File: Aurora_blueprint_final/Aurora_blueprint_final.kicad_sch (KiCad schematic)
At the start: 29 parts, among them J1 Raspberry_Pi_4, K1 FINDER-40.11, K2 FINDER-40.11, K3 FINDER-40.11, K4 FINDER-40.11, M1 Motor_DC, M2 Motor_DC, M3 Motor_DC, M4 Motor_DC, U1 L7805, U2 L7812, U3 L7805, U4 L7805, U5 L7805, U6 L7812, U7 L7812, U8 L7812

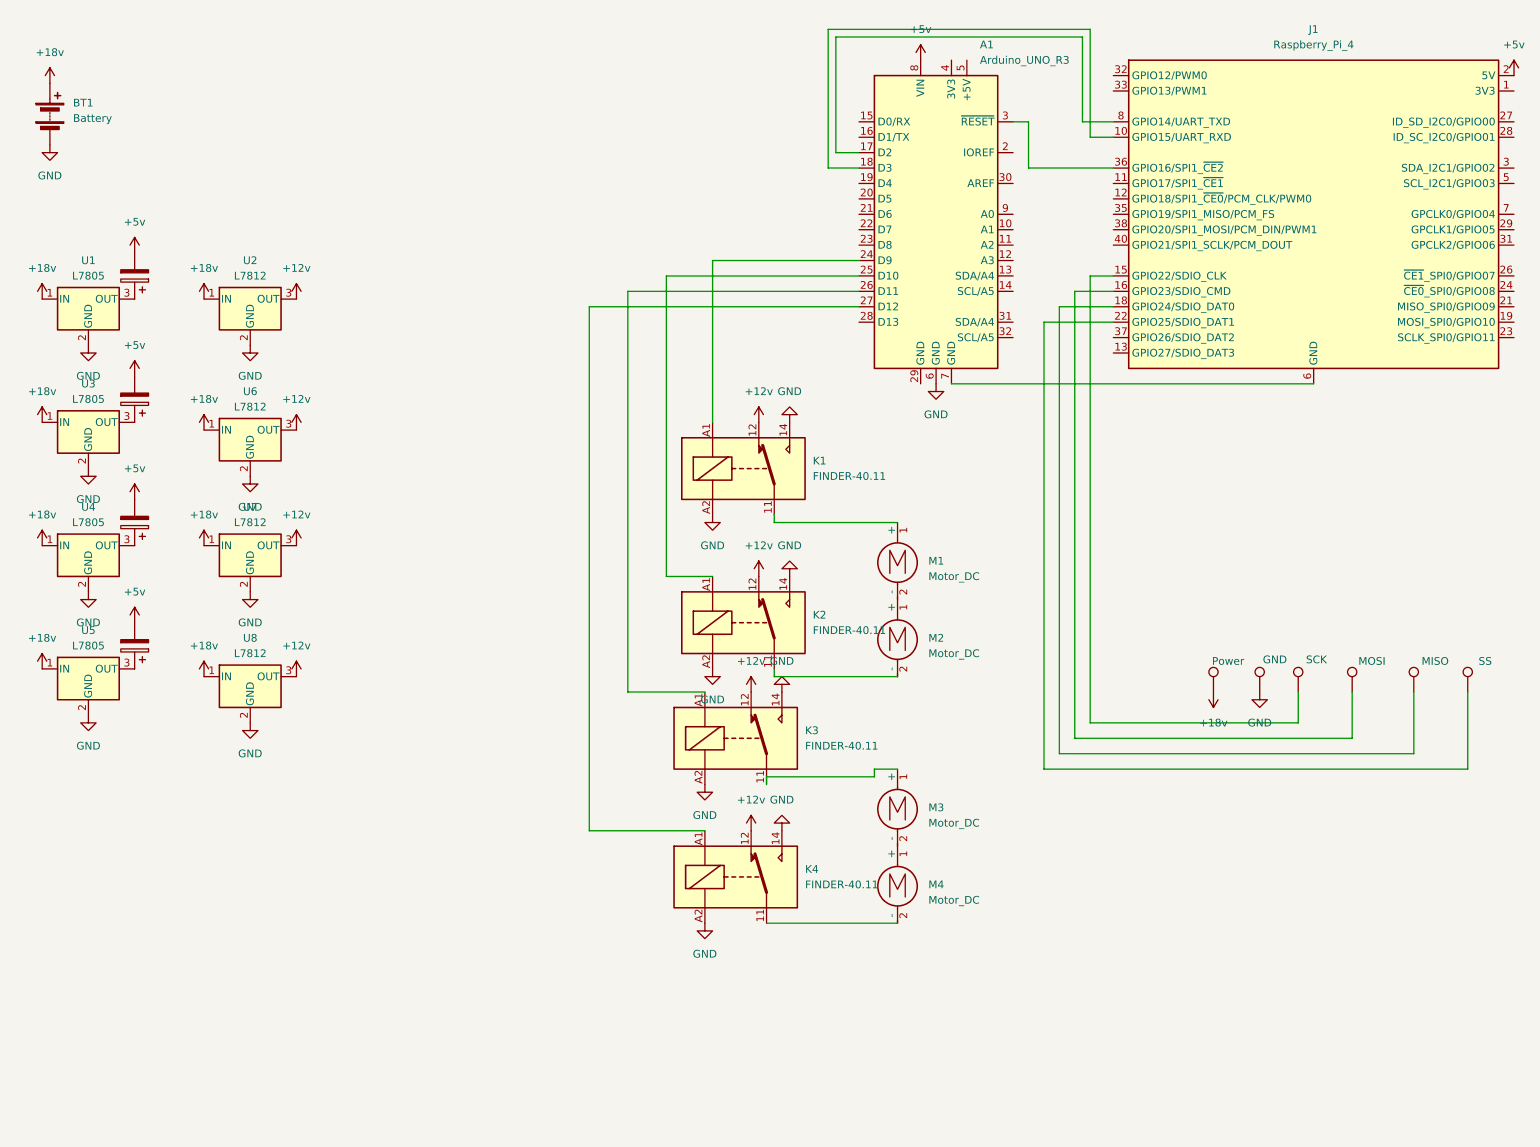
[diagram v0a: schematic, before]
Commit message: Added speedcontrol with arduino provided DPDT relays
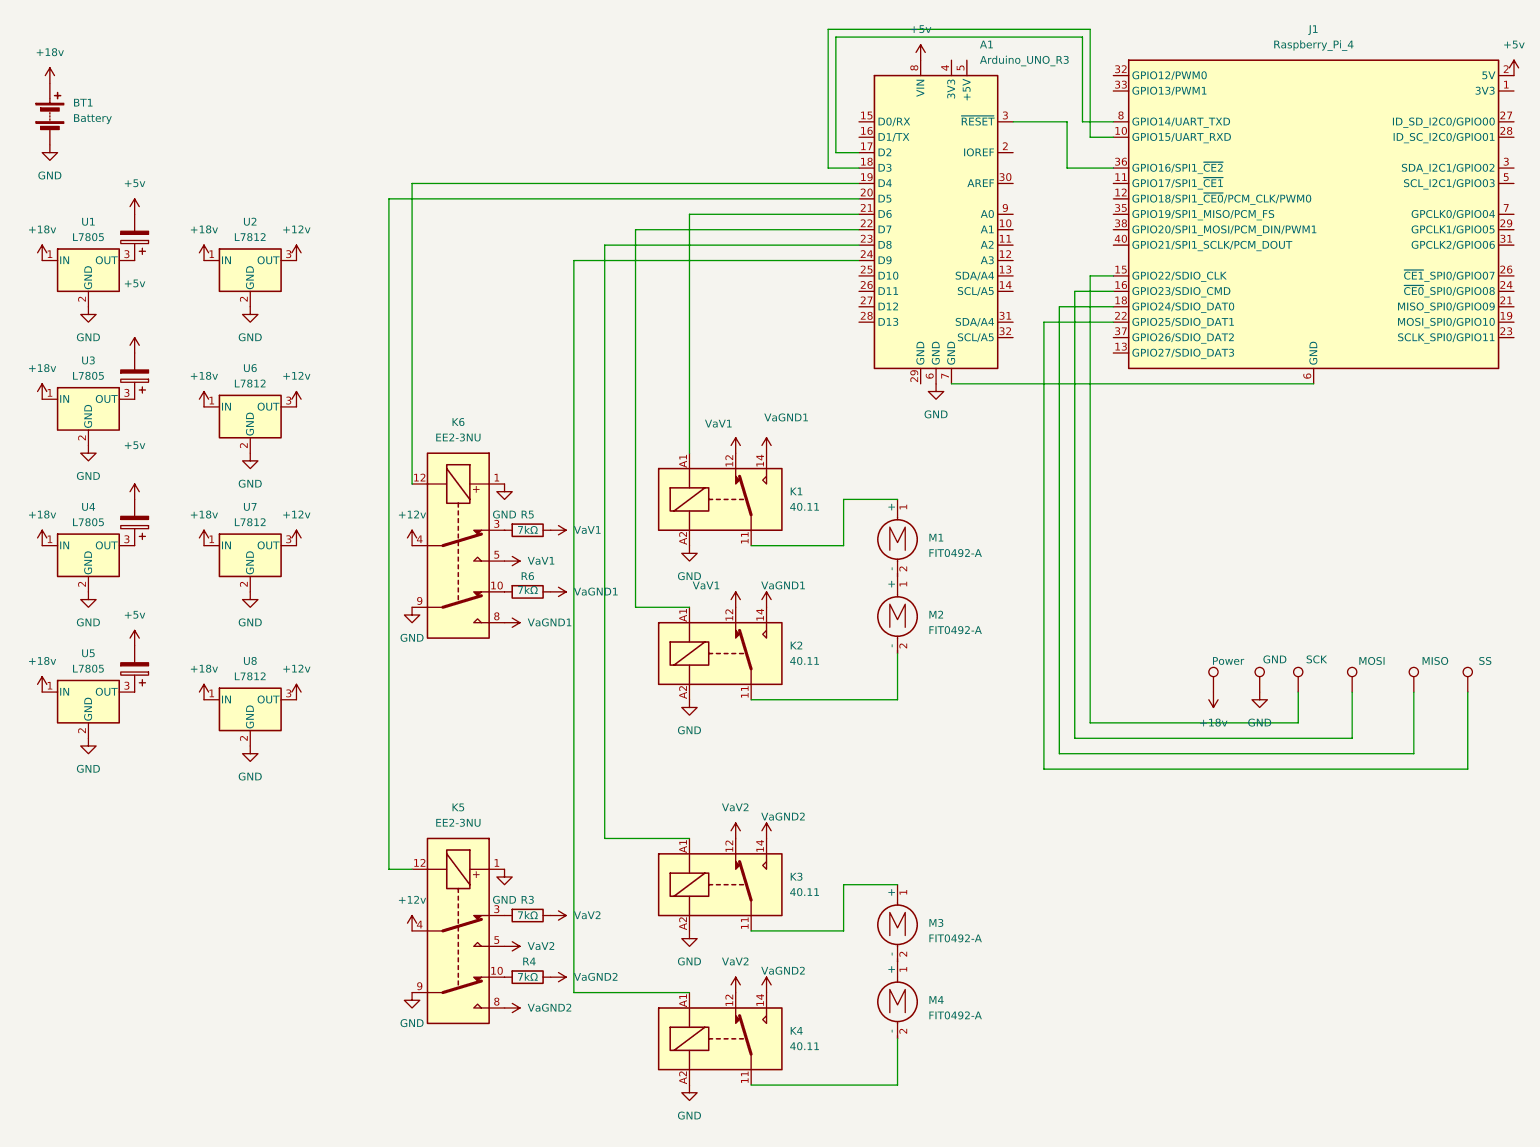
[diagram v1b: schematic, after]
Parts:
- added K5, K6: EE2-3NU, Relay_SMD:Relay_DPDT_Kemet_EE2_NU, symbol Relay:EE2-3NU
- added R3, R4, R5, R6: 7kΩ, symbol Device:R
- K1, K2, K3, K4: value FINDER-40.11 -> 40.11
- M1, M2, M3, M4: value Motor_DC -> FIT0492-A
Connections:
- net +12v: now also K5.4, K6.4; no longer K1.12, K2.12, K3.12, K4.12
- net GND: now also K5.1, K5.9, K6.1, K6.9; no longer K1.14, K2.14, K3.14, K4.14
- net at A1.19 (D4): now also K6.12
- net at A1.20 (D5): now also K5.12
- net at A1.21 (D6): now also K1.A1
- net at A1.22 (D7): now also K2.A1
- net at A1.23 (D8): now also K3.A1
- net at A1.24 (D9): now also K4.A1; no longer K1.A1
- net at A1.25 (D10): no longer K2.A1
- net at A1.26 (D11): no longer K3.A1
- net at A1.27 (D12): no longer K4.A1
- new net: K6.10, R6.2
- new net: K6.3, R5.2
- new net: K5.3, R3.2
- new net: K5.10, R4.2
- new net VaGND1: K1.14, K2.14, K6.8, R6.1
- new net VaGND2: K3.14, K4.14, K5.8, R4.1
- new net VaV1: K1.12, K2.12, K6.5, R5.1
- new net VaV2: K3.12, K4.12, K5.5, R3.1
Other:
- moved on the sheet: K3, K4, M3, M4, U1, U2, U3, U5, U6, U8

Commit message: Stripped arduino of unneeded pins for easier development
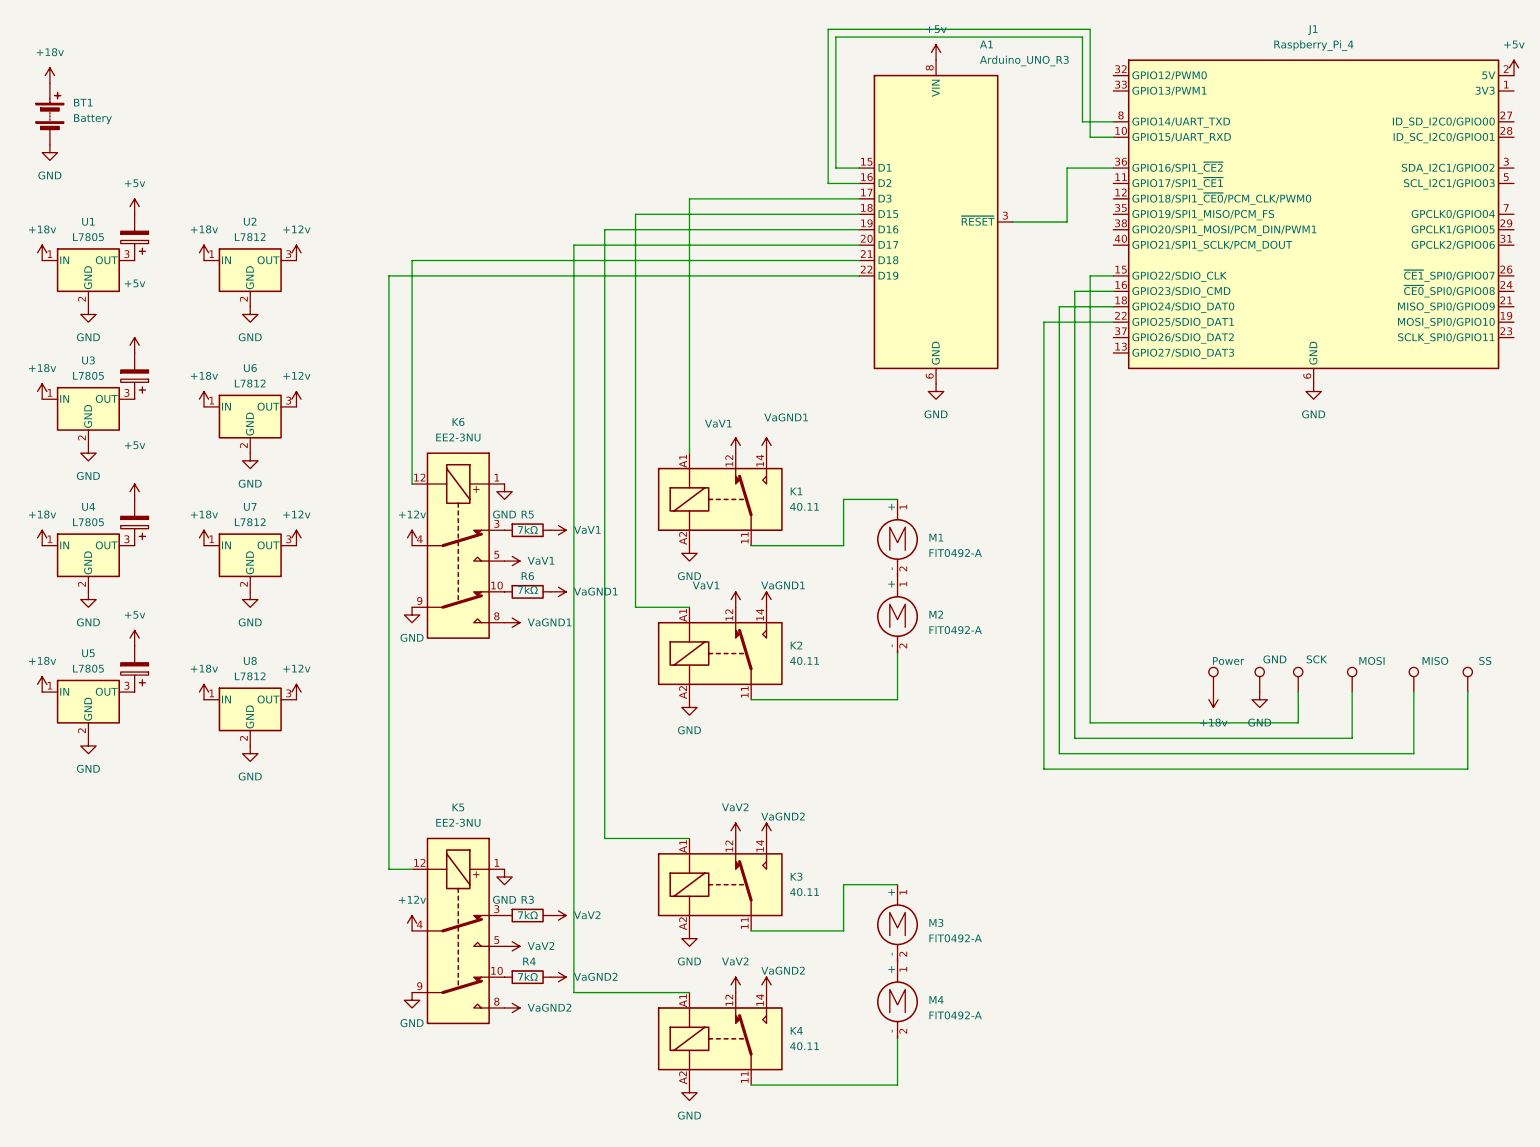
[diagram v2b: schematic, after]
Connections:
- net GND: now also J1.14 (GND), J1.20 (GND), J1.25 (GND), J1.30 (GND), J1.34 (GND), J1.39 (GND), J1.6 (GND), J1.9 (GND)
- net at A1.15 (D1): now also J1.8 (GPIO14/UART_TXD)
- net at A1.16 (D2): now also J1.10 (GPIO15/UART_RXD)
- net at A1.17 (D3): now also K1.A1; no longer J1.8 (GPIO14/UART_TXD)
- net at A1.18 (D15): now also K2.A1; no longer J1.10 (GPIO15/UART_RXD)
- net at A1.19 (D16): now also K3.A1; no longer K6.12
- net at A1.20 (D17): now also K4.A1; no longer K5.12
- net at A1.21 (D18): now also K6.12; no longer K1.A1
- net at A1.22 (D19): now also K5.12; no longer K2.A1

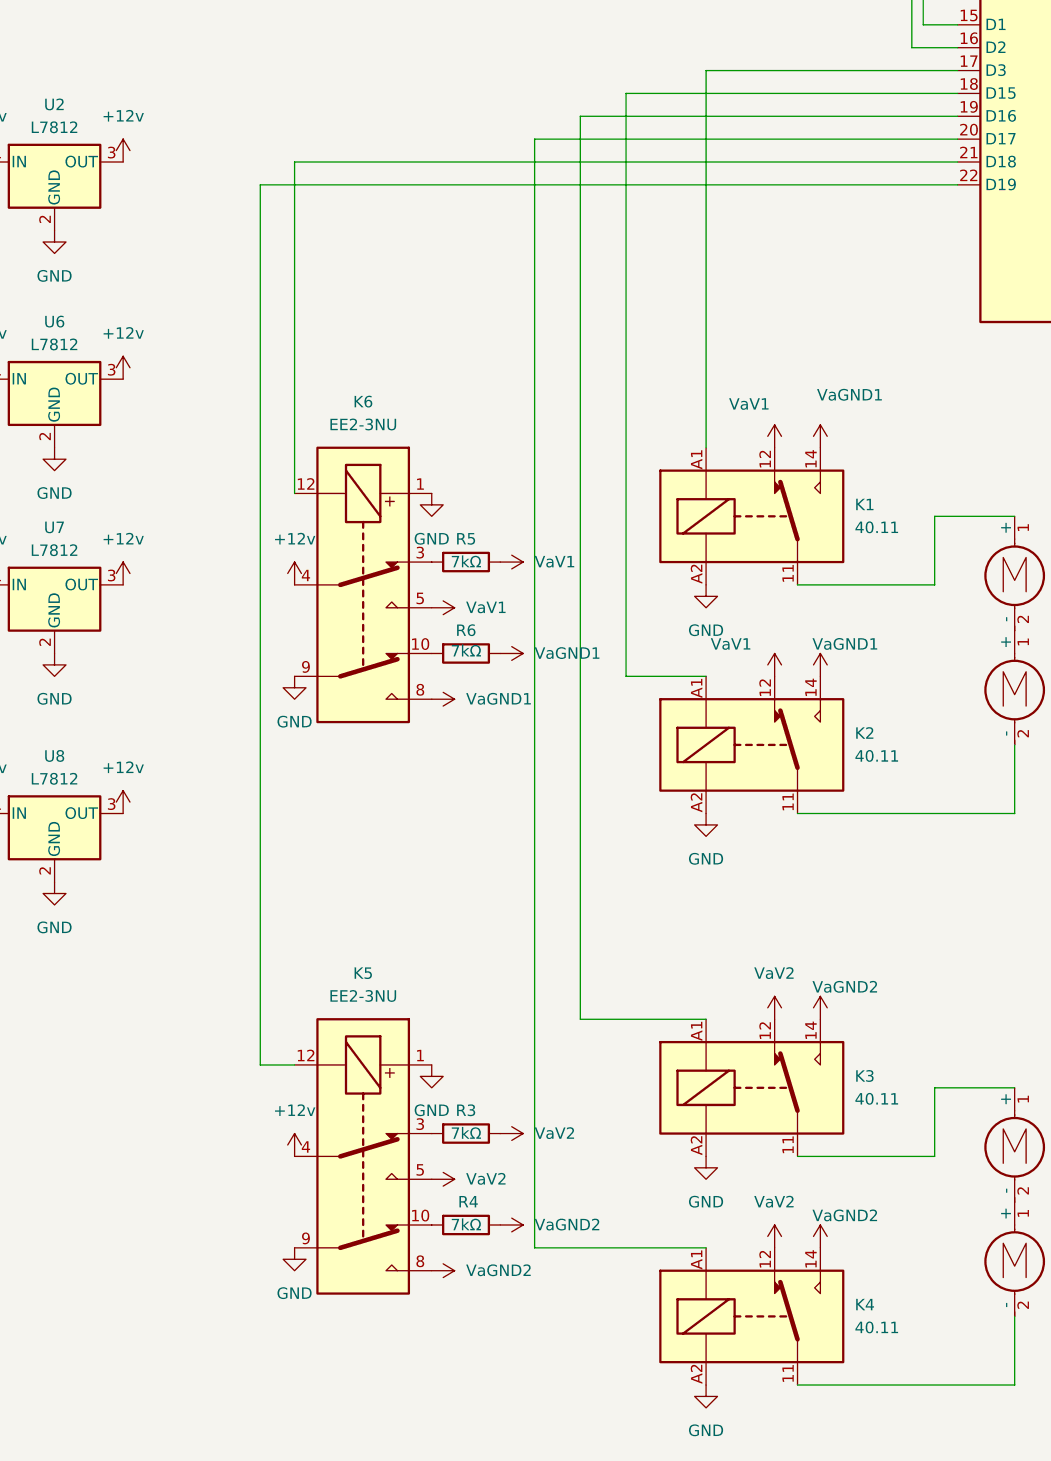
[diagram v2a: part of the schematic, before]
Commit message: Updated cad drawing for better visual clarity
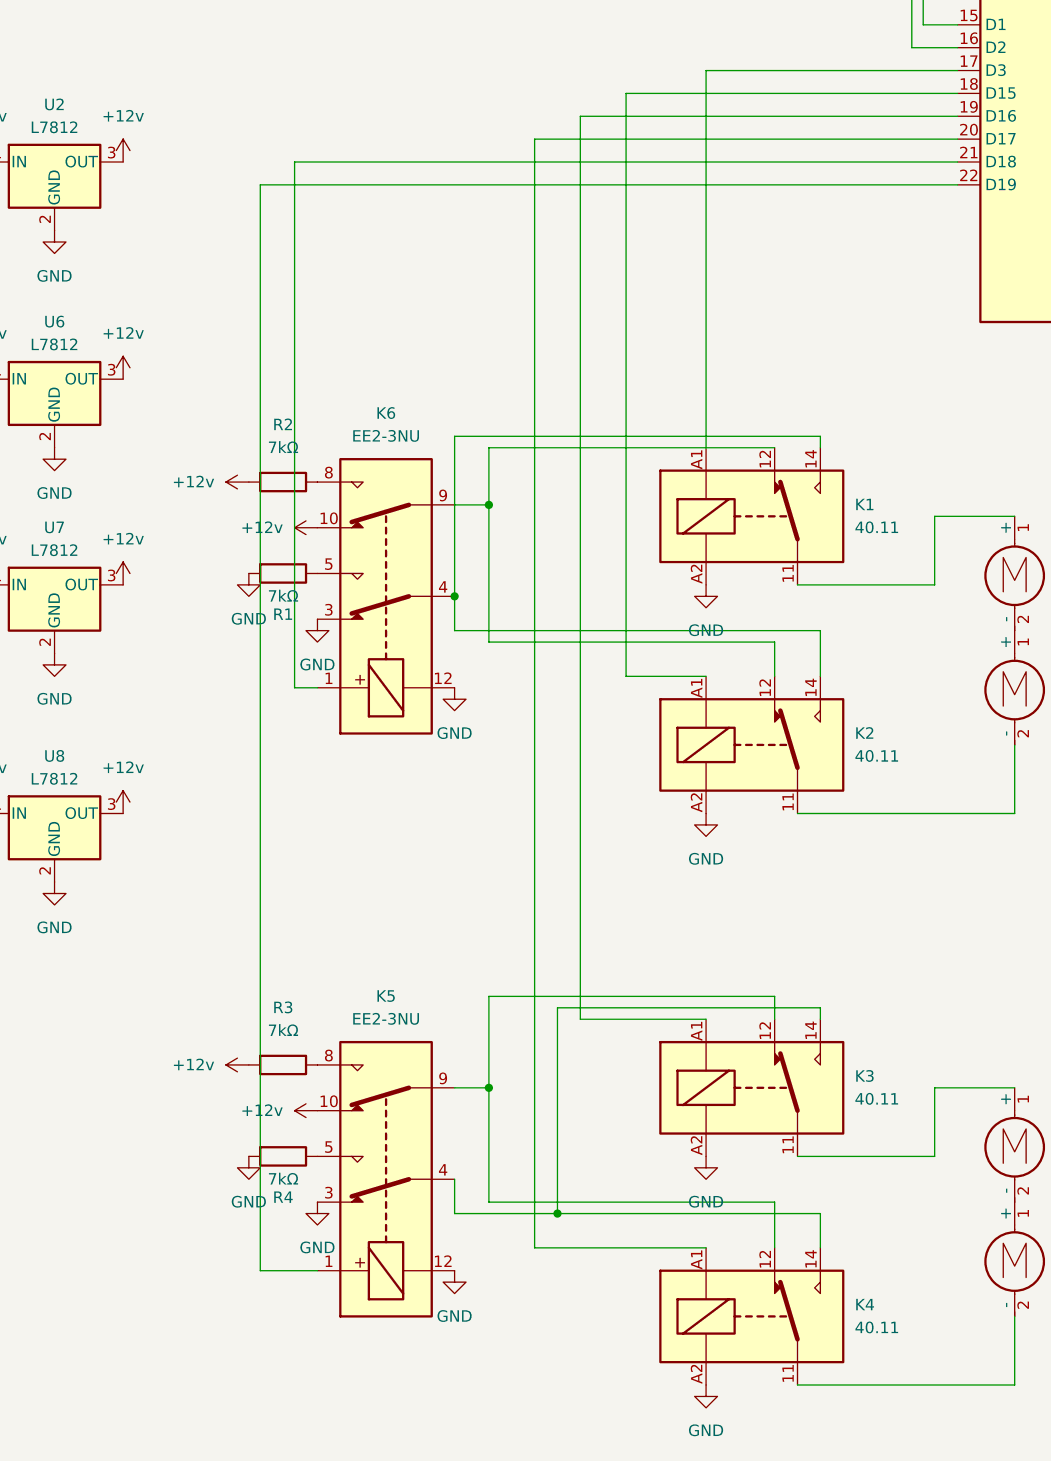
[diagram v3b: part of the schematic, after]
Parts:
- removed R5, R6: 7kΩ, symbol Device:R
- added R1, R2: 7kΩ, symbol Device:R
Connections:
- net +12v: now also K5.10, K6.10, R3.2, R2.2; no longer K5.4, K6.4
- net GND: now also K5.12, K5.3, K6.12, K6.3, R4.2, R1.2; no longer K5.1, K5.9, K6.1, K6.9
- net at A1.21 (D18): now also K6.1; no longer K6.12
- net at A1.22 (D19): now also K5.1; no longer K5.12
- net VaGND1: no longer names the net of K1.14, K2.14
- net VaGND1: now also K6.4; no longer K6.8
- net VaGND2: no longer names the net of K3.14, K4.14
- net VaGND2: now also K5.4; no longer K5.8, R4.1
- net VaV1: no longer names the net of K1.12, K2.12
- net VaV1: now also K6.9; no longer K6.5
- net VaV2: no longer names the net of K3.12, K4.12
- net VaV2: now also K5.9; no longer K5.5, R3.1
- new net: K6.5, R1.1
- new net: K6.8, R2.1
- new net: K5.5, R4.1
- new net: K5.8, R3.1
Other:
- moved on the sheet: K6

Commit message: Revised blueprint
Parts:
- removed A1: Arduino_UNO_R3, Module:Arduino_UNO_R3, symbol MCU_Module:Arduino_UNO_R3
- removed C1, C2, C3, C4: C_Polarized, symbol Device:C_Polarized
- removed GND, MISO, MOSI, SCK, SS: TestPoint, symbol Connector:TestPoint
- removed J1: Raspberry_Pi_4, symbol Connector:Raspberry_Pi_4
- removed K1, K2, K3, K4: 40.11, Relay_THT:Relay_SPDT_Finder_40.11, symbol Relay:FINDER-40.11
- removed K5, K6: EE2-3NU, Relay_SMD:Relay_DPDT_Kemet_EE2_NU, symbol Relay:EE2-3NU
- removed M1, M2, M3, M4: FIT0492-A, symbol Motor:Motor_DC
- removed Power: ~, symbol Connector:TestPoint
- removed R1, R2, R3, R4: 7kΩ, symbol Device:R
- removed U1, U3, U4, U5: L7805, symbol Regulator_Linear:L7805
- removed U2, U6, U7, U8: L7812, symbol Regulator_Linear:L7812
- added A2: Arduino_UNO_R3, Module:Arduino_UNO_R3, symbol MCU_Module:Arduino_UNO_R3
- added BT2: Battery, symbol Device:Battery
- added J2: Raspberry_Pi_4, symbol Connector:Raspberry_Pi_4
- added K10, K11, K7, K8: 40.11, Relay_THT:Relay_SPDT_Finder_40.11, symbol Relay:FINDER-40.11
- added K12, K9: FINDER-36.11, Relay_THT:Relay_SPDT_Finder_36.11, symbol Relay:FINDER-36.11
- added M5, M6, M7, M8: FIT0492-A, symbol Motor:Motor_DC
- added Q5, Q6, Q7, Q8: IRLZ34N, Package_TO_SOT_THT:TO-220-3_Vertical, symbol Transistor_FET:IRLZ34N
- added R10, R11, R12, R7, R8, R9: 2400, symbol Device:R
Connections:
- net +18v: now also K12.12, K9.12, Q5.2 (D), Q6.2 (D), Q7.2 (D), Q8.2 (D), R12.2, R9.2
- net +5v: now also BT2.1 (+)
- net GND: now also BT2.2 (-), J2.14 (GND), J2.20 (GND), J2.25 (GND), J2.30 (GND), J2.34 (GND), J2.39 (GND), J2.6 (GND), J2.9 (GND), K10.A1, K11.A1, K12.A1, K7.A1, K8.A1, K9.A1, R10.1, R11.1, R7.1, R8.1
- new net: K7.14, R7.2
- new net: A2.19 (D16), Q8.1 (G)
- new net: K11.A2, Q8.3 (S)
- new net: J2.1 (3V3), J2.17 (3V3)
- new net: A2.16 (D2), J2.10 (GPIO15/UART_RXD)
- new net: J2.2 (5V), J2.4 (5V)
- new net: A2.3 (~{RESET}), J2.36 (GPIO16/SPI1_~{CE2})
- new net: A2.15 (D1), J2.8 (GPIO14/UART_TXD)
- new net: K7.11, M5.1 (+)
- new net: M5.2 (-), M6.1 (+)
- new net: K7.12, K8.12, K9.11
- new net: K7.A2, Q5.3 (S)
- new net: A2.18 (D15), Q6.1 (G)
- new net: K8.A2, Q6.3 (S)
- new net: K10.14, R10.2
- new net: A2.17 (D3), Q5.1 (G)
- new net: M7.2 (-), M8.1 (+)
- new net: K10.11, M8.2 (-)
- new net: K8.11, M6.2 (-)
- new net: K8.14, R8.2
- new net: K12.14, R12.1
- new net: K9.14, R9.1
- new net: A2.21 (D18), K9.A2
- new net: K11.11, M7.1 (+)
- new net: K11.14, R11.2
- new net: K10.12, K11.12, K12.11
- new net: A2.22 (D19), K12.A2
- new net: A2.20 (D17), Q7.1 (G)
- new net: K10.A2, Q7.3 (S)
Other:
- moved on the sheet: BT1
